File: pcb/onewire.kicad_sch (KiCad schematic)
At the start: 7 parts, among them J15 Conn_01x03, J16 Conn_01x03, J17 Screw_Terminal_01x03, Q1 BSS138, U1 DS18B20

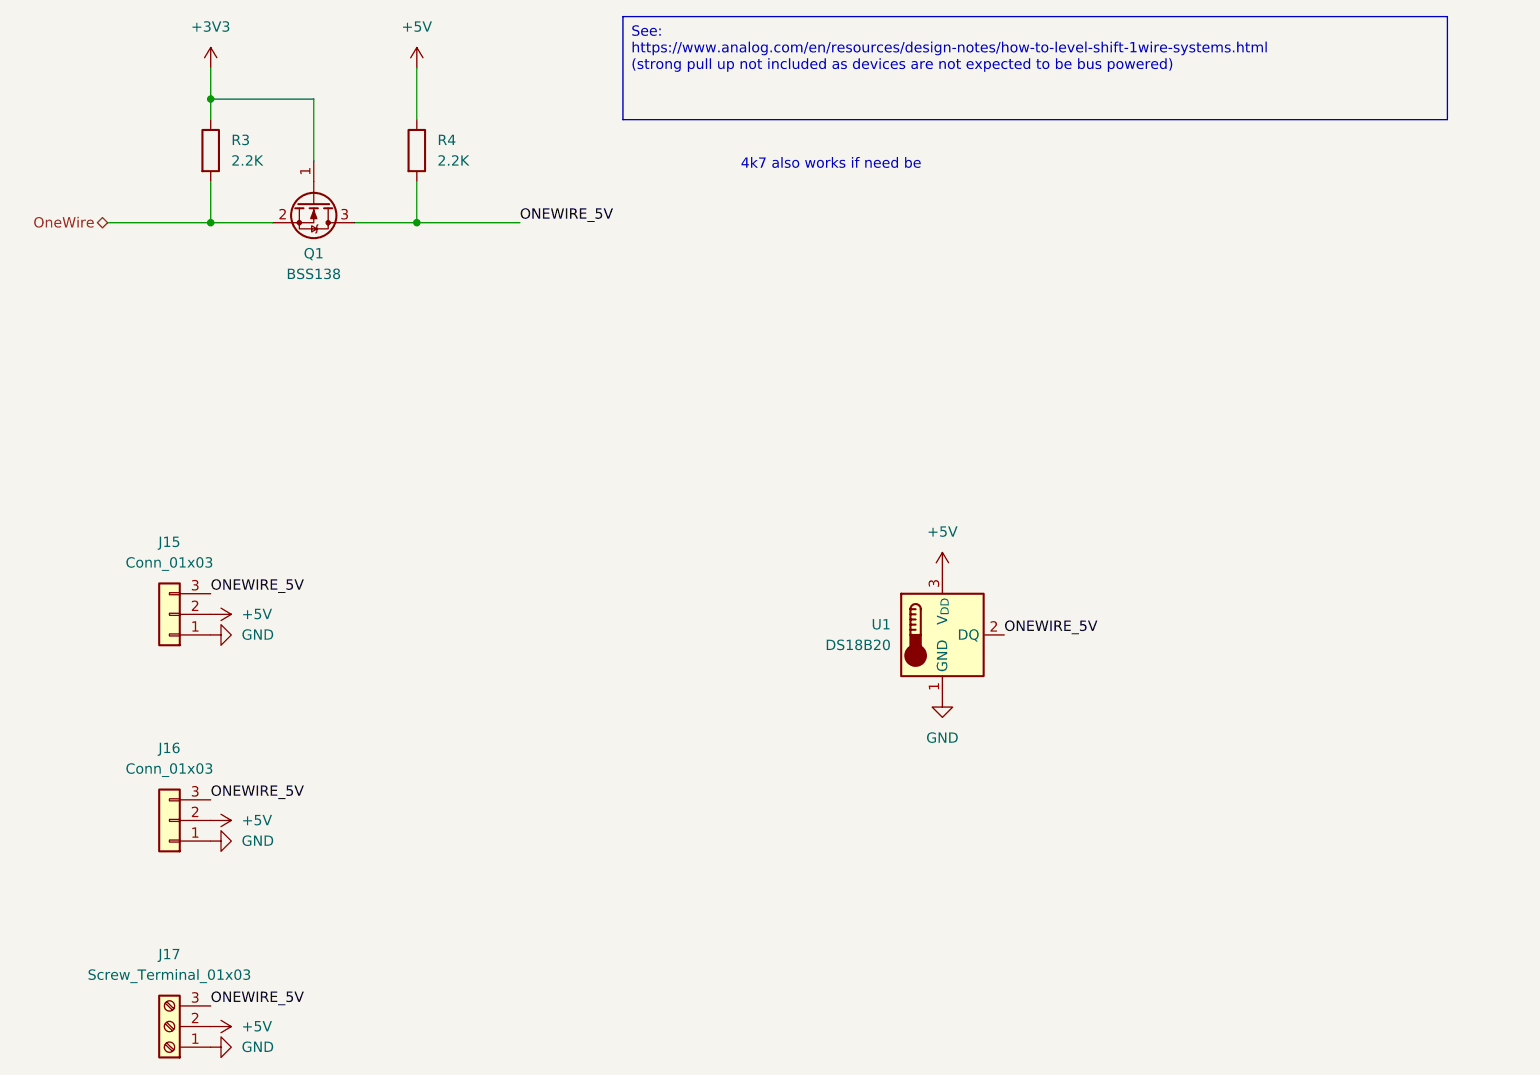
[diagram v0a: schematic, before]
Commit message: Convert PCB to KiCad 9.0 format
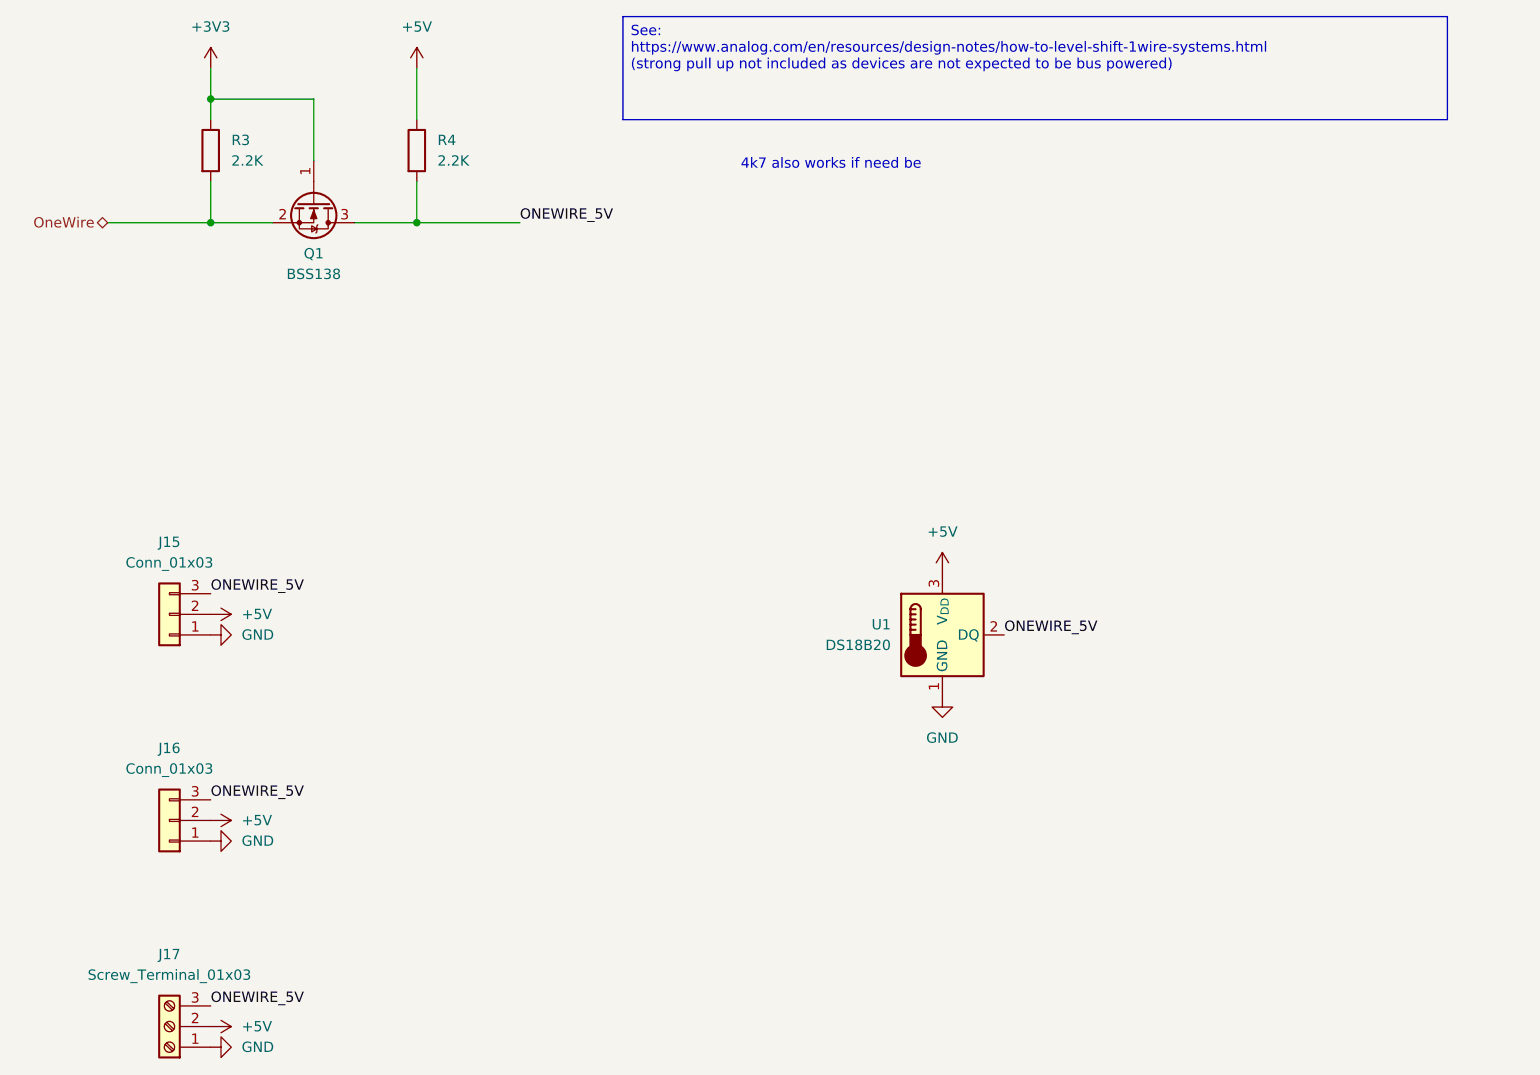
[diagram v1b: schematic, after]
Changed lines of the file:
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@@
 (kicad_sch
-	(version 20231120)
+	(version 20250114)
 	(generator "eeschema")
-	(generator_version "8.0")
+	(generator_version "9.0")
 	(paper "A4")
+	(text "4k7 also works if need be"
+		(exclude_from_sim no)
+		(at 152.654 56.388 0)
+		(effects
+			(font
+				(size 1.27 1.27)
+			)
+		)
+	)
+	(text_box "See:\nhttps://www.analog.com/en/resources/design-notes/how-to-level-shift-1wire-systems.html\n(strong pull up not included as devices are not expected to be bus powered)"
+		(exclude_from_sim no)
+		(at 127 38.1 0)
+		(size 101.6 12.7)
+		(margins 0.9525 0.9525 0.9525 0.9525)
+		(stroke
+			(width 0)
+			(type default)
+		)
+		(fill
+			(type none)
+		)
+		(effects
+			(font
+				(size 1.27 1.27)
+			)
+			(justify left top)
+		)
+	)
 	(junction
 		(at 101.6 63.5)
@@
 		)
 	)
-	(text_box "See:\nhttps://www.analog.com/en/resources/design-notes/how-to-level-shift-1wire-systems.html\n(strong pull up not included as devices are not expected to be bus powered)"
-		(exclude_from_sim no)
-		(at 127 38.1 0)
-		(size 101.6 12.7)
-		(stroke
-			(width 0)
-			(type default)
-		)
-		(fill
-			(type none)
-		)
-		(effects
-			(font
-				(size 1.27 1.27)
-			)
-			(justify left top)
-		)
-	)
-	(text "4k7 also works if need be"
-		(exclude_from_sim no)
-		(at 152.654 56.388 0)
-		(effects
-			(font
-				(size 1.27 1.27)
-			)
-		)
-	)
 	(label "ONEWIRE_5V"
 		(at 173.99 114.3 0)
-		(fields_autoplaced yes)
 		(effects
 			(font
@@
 	(label "ONEWIRE_5V"
 		(at 76.2 160.02 0)
-		(fields_autoplaced yes)
 		(effects
 			(font
@@
 	(label "ONEWIRE_5V"
 		(at 114.3 63.5 0)
-		(fields_autoplaced yes)
 		(effects
 			(font
@@
 	(label "ONEWIRE_5V"
 		(at 76.2 109.22 0)
-		(fields_autoplaced yes)
 		(effects
 			(font
@@
 	(label "ONEWIRE_5V"
 		(at 76.2 134.62 0)
-		(fields_autoplaced yes)
 		(effects
 			(font
@@
 		(shape bidirectional)
 		(at 63.5 63.5 180)
-		(fields_autoplaced yes)
 		(effects
 			(font
